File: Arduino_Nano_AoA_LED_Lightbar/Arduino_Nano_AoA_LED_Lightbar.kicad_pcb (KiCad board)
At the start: 2 copper layers, 30 x 70 mm, 17 parts, among them J1 Conn_01x09_Pin

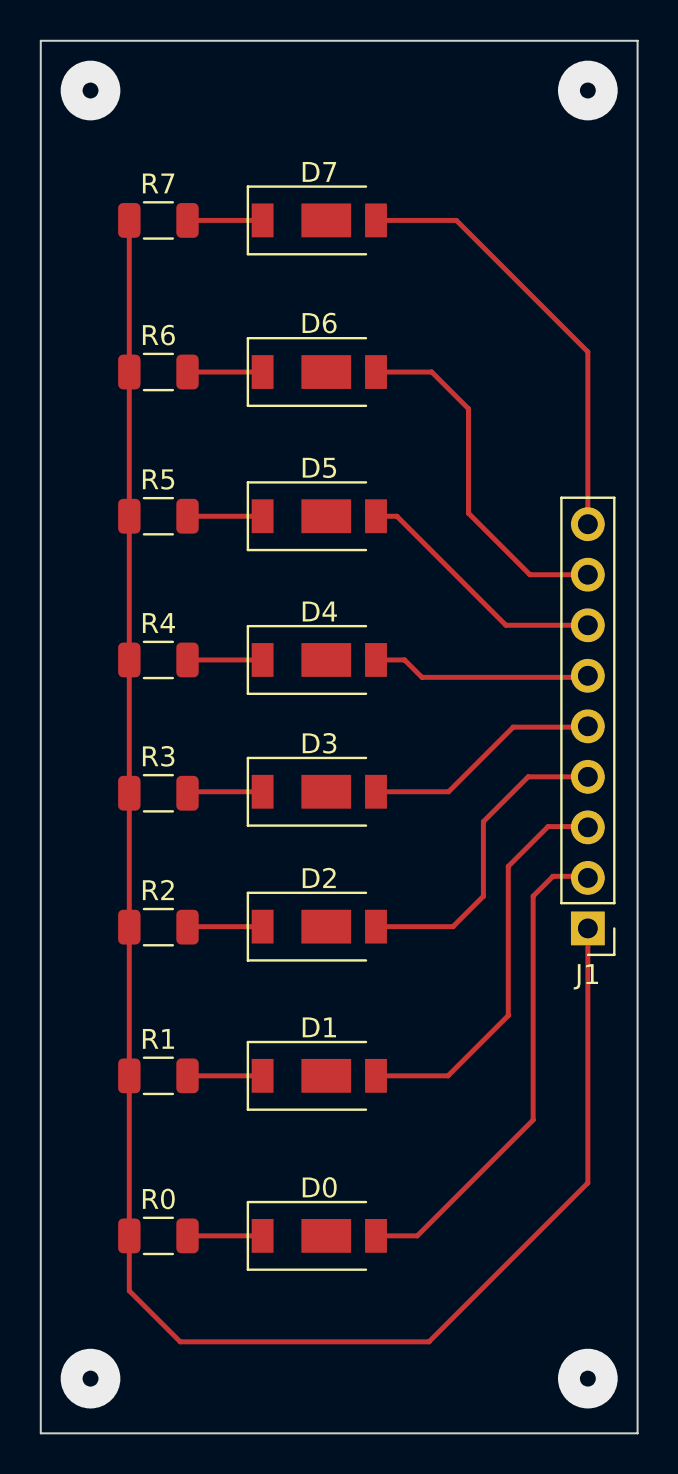
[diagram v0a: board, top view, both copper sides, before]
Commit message: Created a new board for the Wit-Motion WT901B IMU chip.
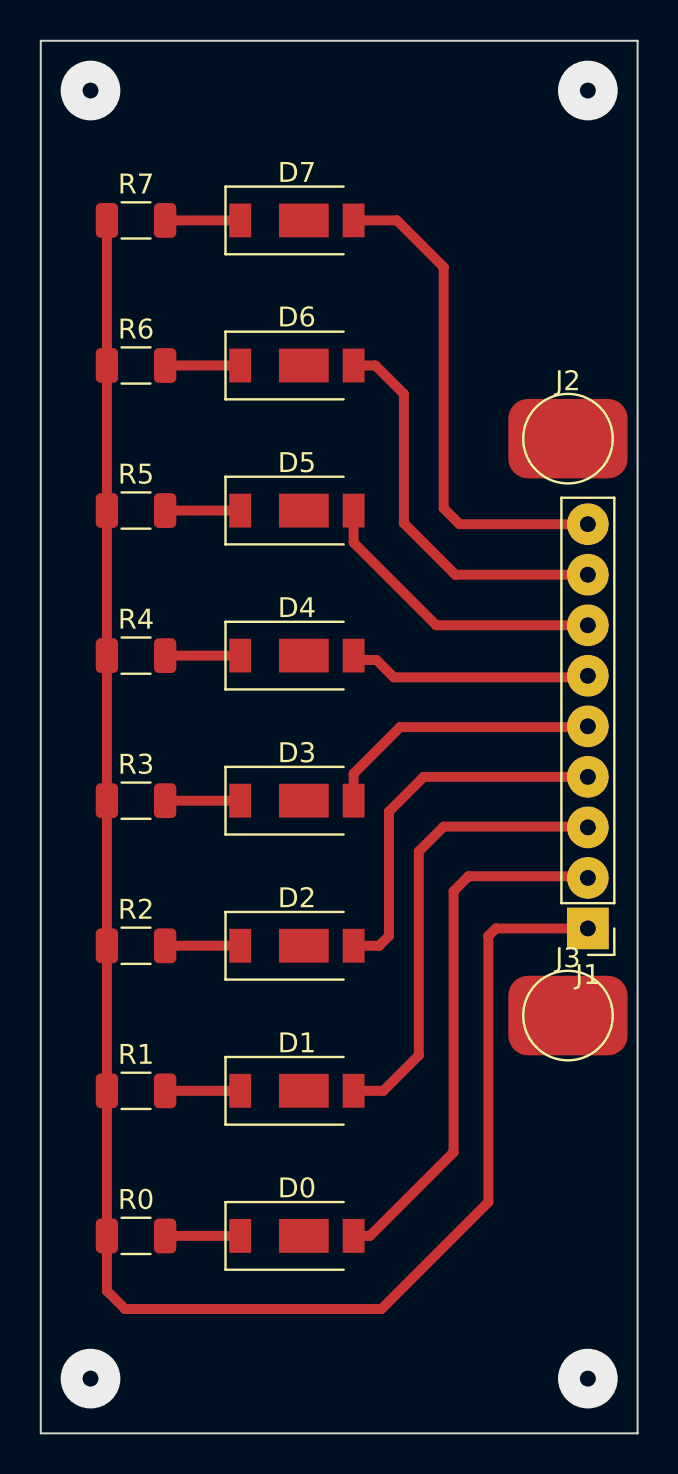
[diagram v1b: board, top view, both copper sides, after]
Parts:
- added J2: SolderPad2, TestPoint:TestPoint_Pad_D4.0mm, F.Cu at (95.5, 84.1)
- added J3: SolderPad1, TestPoint:TestPoint_Pad_D4.0mm, F.Cu at (95.5, 113.1)
- moved D2 1.48 mm to (81.9, 109.6)
- moved R2 1.46 mm to (73.8, 109.6)
- moved D1 1.35 mm to (81.9, 116.9)
- moved R1 1.35 mm to (73.8, 116.9)
- moved D3 1.21 mm to (81.9, 102.3)
- moved R3 1.19 mm to (73.8, 102.3)
- moved D6 1.17 mm to (81.9, 80.4)
- moved R6 1.17 mm to (73.8, 80.4)
- moved D5 1.16 mm to (81.9, 87.7)
- moved R5 1.16 mm to (73.8, 87.7)
- moved D4 1.15 mm to (81.9, 95.0)
- moved R4 1.15 mm to (73.8, 95.0)
- moved D0 1.12 mm to (81.9, 124.2)
- moved D7 1.12 mm to (81.9, 73.2)
- moved R0 1.12 mm to (73.8, 124.2)
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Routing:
- net Net-(D7-A): track 22.0 -> 25.2 mm
- net Net-(D1-A): track 20.3 -> 23.3 mm
- net Net-(D2-A): track 16.0 -> 19.0 mm
- net Net-(D0-A): track 24.8 -> 27.0 mm
- net Net-(D6-A): track 17.9 -> 19.9 mm
- net Net-(D5-A): track 12.9 -> 14.8 mm
- net Net-(D3-A): track 12.0 -> 13.7 mm
- net Net-(D4-A): track 11.0 -> 12.2 mm
- net Net-(D4-K): track 4.31 -> 3.77 mm
